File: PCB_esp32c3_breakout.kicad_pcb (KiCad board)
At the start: 4 copper layers, 19.6 x 44.5 mm, 4 parts, among them J1 Conn_01x09_Pin, J2 Conn_01x09_Pin, U1 ESP32-C3-WROOM-02

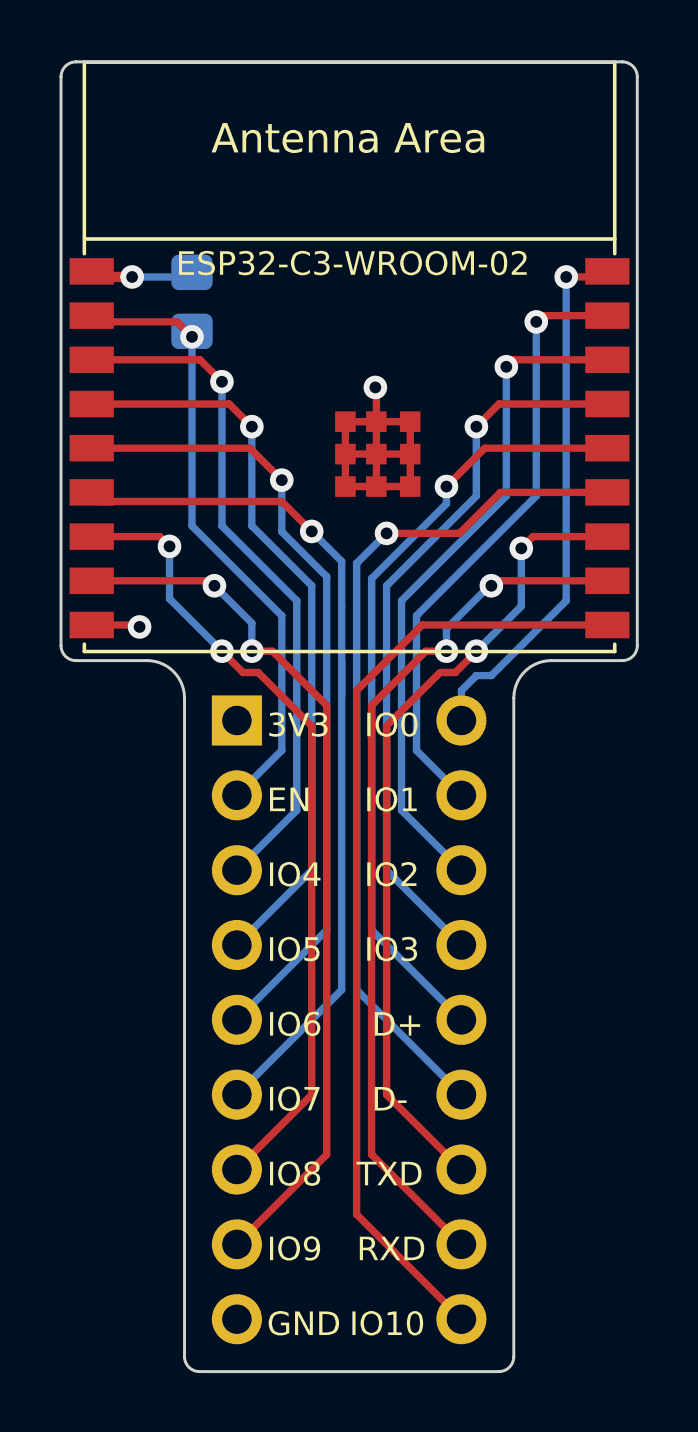
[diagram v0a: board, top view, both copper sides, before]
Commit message: Adjust board size
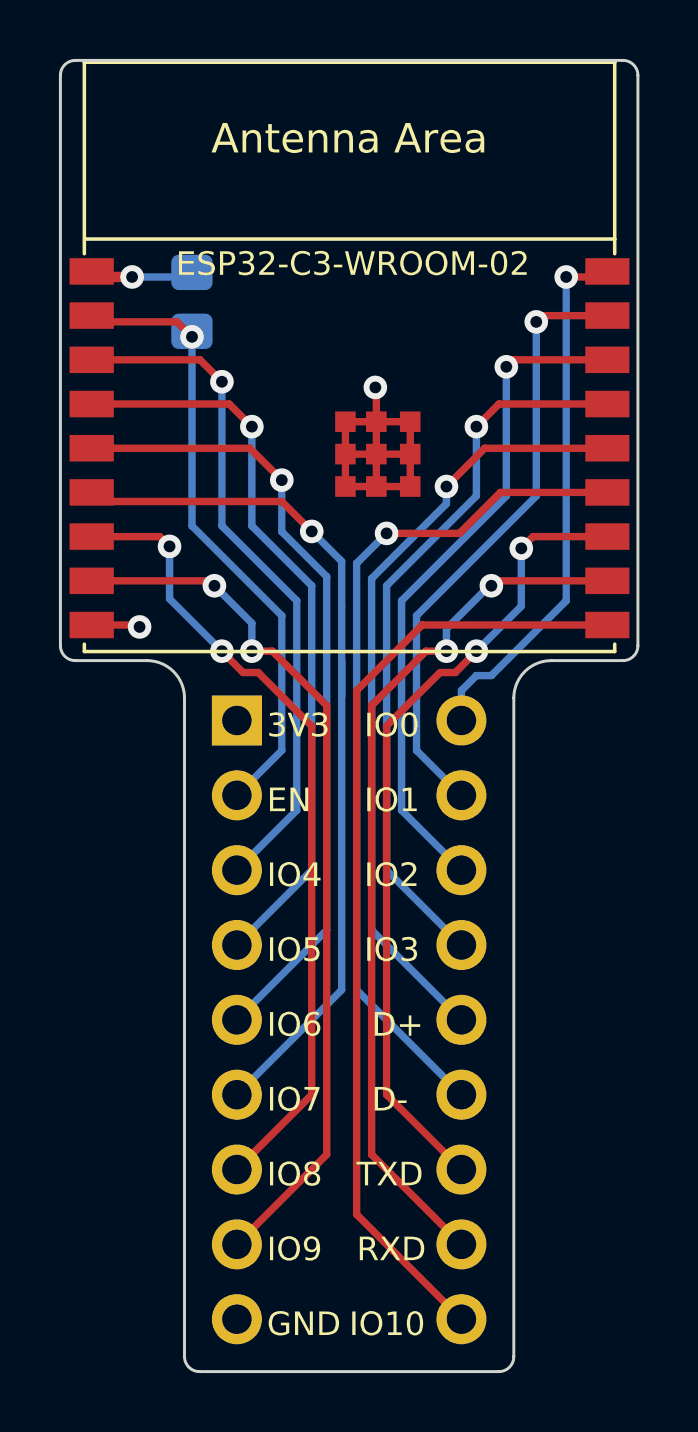
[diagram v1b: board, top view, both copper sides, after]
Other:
- outline, holes or cut-outs redrawn
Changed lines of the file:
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@@
   (title_block
     (title "ESP32-C3-WROOM-02 Breakout Board")
-    (date "2024-02-11")
-    (rev "1.1")
+    (date "2024-02-23")
+    (rev "1.1.1")
     (company "K.Takata")
   )
@@
     )
   )
-  (gr_arc (start 79.629 58.42) (mid 79.48021 58.77921) (end 79.121 58.928)
+  (gr_arc (start 79.65 58.42) (mid 79.501211 58.779211) (end 79.142 58.928)
     (stroke (width 0.1) (type default)) (layer "Edge.Cuts"))
   (gr_line (start 64.77 83.058) (end 74.93 83.058)
     (stroke (width 0.1) (type default)) (layer "Edge.Cuts"))
-  (gr_line (start 76.708 58.928) (end 79.121 58.928)
+  (gr_line (start 76.708 58.928) (end 79.142 58.928)
     (stroke (width 0.1) (type default)) (layer "Edge.Cuts"))
   (gr_arc (start 64.77 83.058) (mid 64.41079 82.90921) (end 64.262 82.55)
     (stroke (width 0.1) (type default)) (layer "Edge.Cuts"))
-  (gr_arc (start 60.579 58.928) (mid 60.21979 58.77921) (end 60.071 58.42)
-    (stroke (width 0.1) (type default)) (layer "Edge.Cuts"))
-  (gr_line (start 79.629 58.42) (end 79.629 39.116)
+  (gr_arc (start 60.558 58.928) (mid 60.198789 58.779211) (end 60.05 58.42)
+    (stroke (width 0.1) (type default)) (layer "Edge.Cuts"))
+  (gr_line (start 79.65 58.42) (end 79.65 39.066)
     (stroke (width 0.1) (type default)) (layer "Edge.Cuts"))
   (gr_arc (start 75.438 82.55) (mid 75.28921 82.90921) (end 74.93 83.058)
     (stroke (width 0.1) (type default)) (layer "Edge.Cuts"))
-  (gr_line (start 60.579 58.928) (end 62.992 58.928)
+  (gr_line (start 60.558 58.928) (end 62.992 58.928)
     (stroke (width 0.1) (type default)) (layer "Edge.Cuts"))
   (gr_line (start 64.262 60.198) (end 64.262 82.55)
     (stroke (width 0.1) (type default)) (layer "Edge.Cuts"))
-  (gr_line (start 79.121 38.608) (end 60.579 38.608)
-    (stroke (width 0.1) (type default)) (layer "Edge.Cuts"))
-  (gr_line (start 60.071 39.116) (end 60.071 58.42)
-    (stroke (width 0.1) (type default)) (layer "Edge.Cuts"))
-  (gr_arc (start 60.071 39.116) (mid 60.21979 38.75679) (end 60.579 38.608)
+  (gr_line (start 79.142 38.558) (end 60.558 38.558)
+    (stroke (width 0.1) (type default)) (layer "Edge.Cuts"))
+  (gr_line (start 60.05 39.066) (end 60.05 58.42)
+    (stroke (width 0.1) (type default)) (layer "Edge.Cuts"))
+  (gr_arc (start 60.05 39.066) (mid 60.198789 38.706789) (end 60.558 38.558)
     (stroke (width 0.1) (type default)) (layer "Edge.Cuts"))
   (gr_arc (start 75.438 60.198) (mid 75.809974 59.299974) (end 76.708 58.928)
@@
   (gr_line (start 75.438 82.55) (end 75.438 60.198)
     (stroke (width 0.1) (type default)) (layer "Edge.Cuts"))
-  (gr_arc (start 79.121 38.608) (mid 79.48021 38.75679) (end 79.629 39.116)
+  (gr_arc (start 79.142 38.558) (mid 79.501211 38.706789) (end 79.65 39.066)
     (stroke (width 0.1) (type default)) (layer "Edge.Cuts"))
   (gr_arc (start 62.992 58.928) (mid 63.890026 59.299974) (end 64.262 60.198)
@@
   )
   (dimension (type aligned) (layer "Dwgs.User")
-    (pts (xy 60.071 39.116) (xy 79.629 39.116))
-    (height -2.413)
-    (gr_text "19.5580 mm" (at 69.85 35.553) (layer "Dwgs.User")
+    (pts (xy 69.85 38.558) (xy 69.85 83.058))
+    (height 11.43)
+    (gr_text "44.5000 mm" (at 57.27 60.808 90) (layer "Dwgs.User")
       (effects (font (size 1 1) (thickness 0.15)))
     )
@@
   )
   (dimension (type aligned) (layer "Dwgs.User")
-    (pts (xy 69.85 38.608) (xy 69.85 83.058))
-    (height 11.728022)
-    (gr_text "44.4500 mm" (at 56.971978 60.833 90) (layer "Dwgs.User")
+    (pts (xy 60.05 39.116) (xy 79.65 39.116))
+    (height -2.286)
+    (gr_text "19.6000 mm" (at 69.85 35.68) (layer "Dwgs.User")
       (effects (font (size 1 1) (thickness 0.15)))
     )
